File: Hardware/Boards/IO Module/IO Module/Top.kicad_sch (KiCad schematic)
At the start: 0 parts

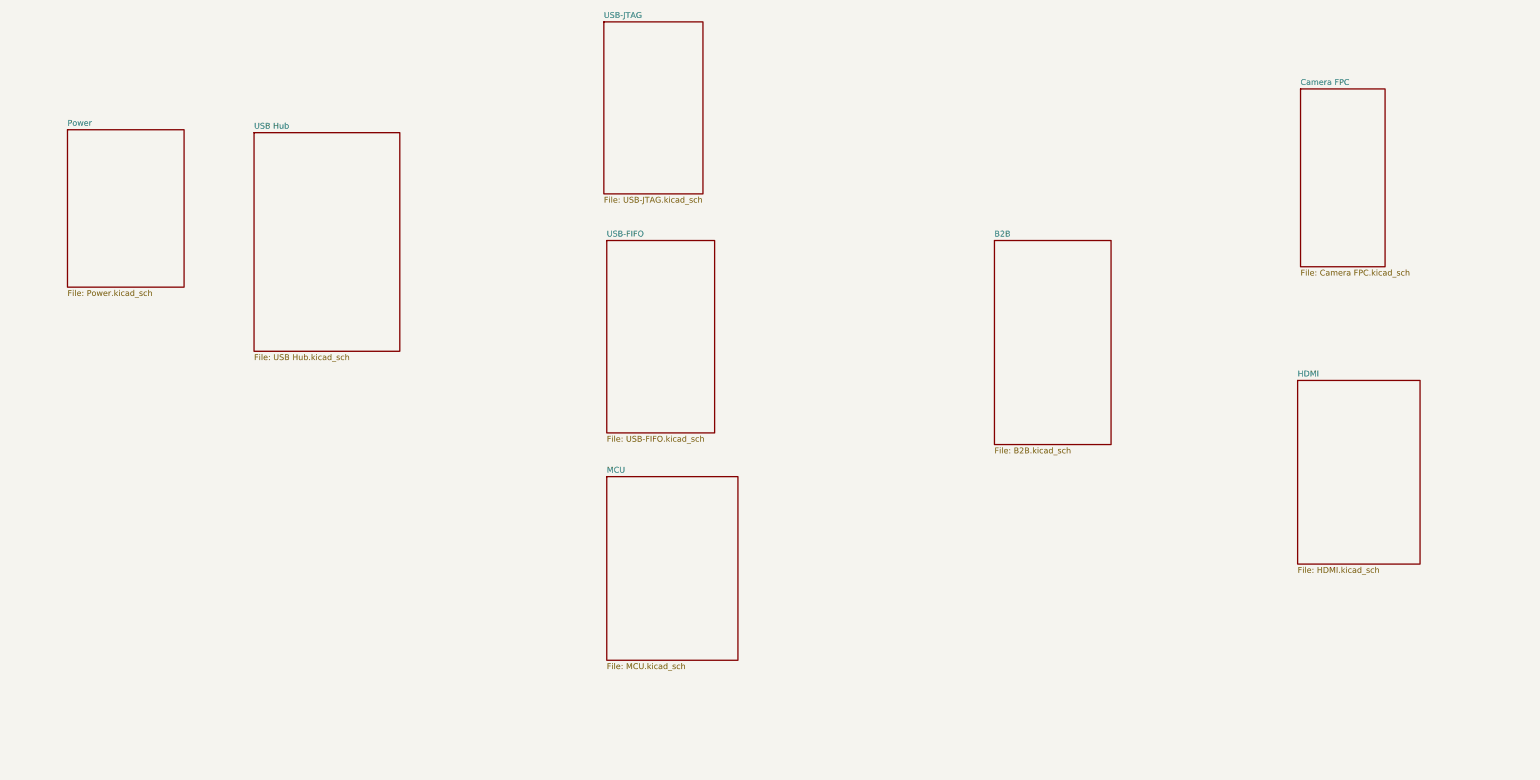
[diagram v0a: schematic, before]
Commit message: Completed IO Module Schematics
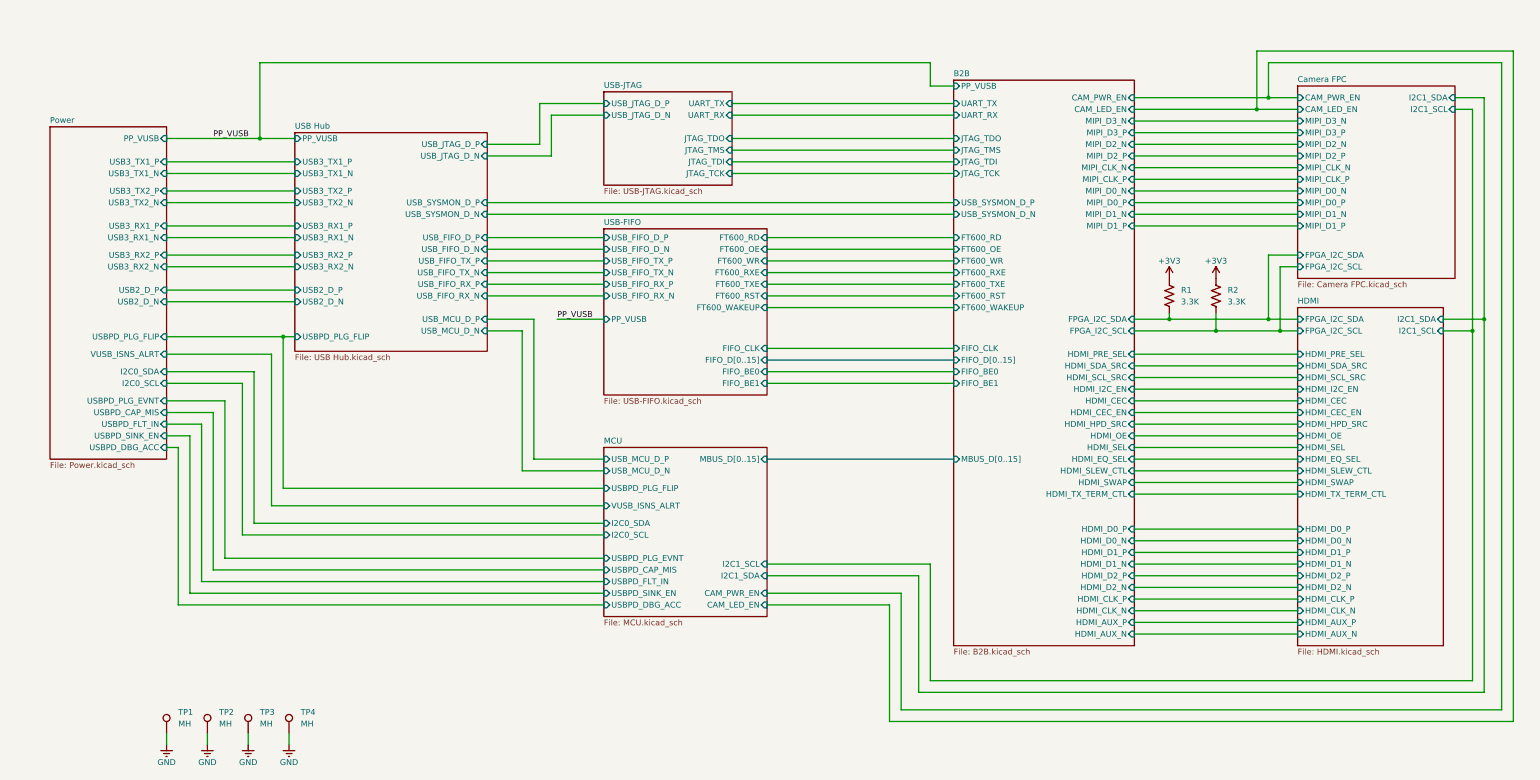
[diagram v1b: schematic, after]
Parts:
- added R1, R2: 3.3K, Resistor_SMD:R_0402_1005Metric, symbol Device:R_US
- added TP1, TP2, TP3, TP4: MH, MountingHole:MountingHole_2.2mm_M2_Pad_Via, symbol Connector:TestPoint
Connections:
- new net +3V3: R1.2, R2.2
- new net B2B/FPGA_I2C_SCL: R2.1
- new net B2B/FPGA_I2C_SDA: R1.1
- new net GND: TP1.1, TP2.1, TP3.1, TP4.1
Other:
- sheet B2B ports: added CAM_LED_EN, CAM_PWR_EN, FIFO_BE0, FIFO_BE1, FIFO_CLK, FIFO_D[0..15], FPGA_I2C_SCL, FPGA_I2C_SDA, FT600_OE, FT600_RD, FT600_RST, FT600_RXE, FT600_TXE, FT600_WAKEUP, FT600_WR, HDMI_AUX_N, HDMI_AUX_P, HDMI_CEC, HDMI_CEC_EN, HDMI_CLK_N, HDMI_CLK_P, HDMI_D0_N, HDMI_D0_P, HDMI_D1_N, HDMI_D1_P, HDMI_D2_N, HDMI_D2_P, HDMI_EQ_SEL, HDMI_HPD_SRC, HDMI_I2C_EN, HDMI_OE, HDMI_PRE_SEL, HDMI_SCL_SRC, HDMI_SDA_SRC, HDMI_SEL, HDMI_SLEW_CTL, HDMI_SWAP, HDMI_TX_TERM_CTL, JTAG_TCK, JTAG_TDI, JTAG_TDO, JTAG_TMS, MBUS_D[0..15], MIPI_CLK_N, MIPI_CLK_P, MIPI_D0_N, MIPI_D0_P, MIPI_D1_N, MIPI_D1_P, MIPI_D2_N, MIPI_D2_P, MIPI_D3_N, MIPI_D3_P, PP_VUSB, UART_RX, UART_TX, USB_SYSMON_D_N, USB_SYSMON_D_P; removed none
- sheet Camera FPC ports: added CAM_LED_EN, CAM_PWR_EN, FPGA_I2C_SCL, FPGA_I2C_SDA, I2C1_SCL, I2C1_SDA, MIPI_CLK_N, MIPI_CLK_P, MIPI_D0_N, MIPI_D0_P, MIPI_D1_N, MIPI_D1_P, MIPI_D2_N, MIPI_D2_P, MIPI_D3_N, MIPI_D3_P; removed none
- sheet HDMI ports: added FPGA_I2C_SCL, FPGA_I2C_SDA, HDMI_AUX_N, HDMI_AUX_P, HDMI_CEC, HDMI_CEC_EN, HDMI_CLK_N, HDMI_CLK_P, HDMI_D0_N, HDMI_D0_P, HDMI_D1_N, HDMI_D1_P, HDMI_D2_N, HDMI_D2_P, HDMI_EQ_SEL, HDMI_HPD_SRC, HDMI_I2C_EN, HDMI_OE, HDMI_PRE_SEL, HDMI_SCL_SRC, HDMI_SDA_SRC, HDMI_SEL, HDMI_SLEW_CTL, HDMI_SWAP, HDMI_TX_TERM_CTL, I2C1_SCL, I2C1_SDA; removed none
- sheet MCU ports: added CAM_LED_EN, CAM_PWR_EN, I2C0_SCL, I2C0_SDA, I2C1_SCL, I2C1_SDA, MBUS_D[0..15], USBPD_CAP_MIS, USBPD_DBG_ACC, USBPD_FLT_IN, USBPD_PLG_EVNT, USBPD_PLG_FLIP, USBPD_SINK_EN, USB_MCU_D_N, USB_MCU_D_P, VUSB_ISNS_ALRT; removed none
- sheet Power ports: added I2C0_SCL, I2C0_SDA, PP_VUSB, USB2_D_N, USB2_D_P, USB3_RX1_N, USB3_RX1_P, USB3_RX2_N, USB3_RX2_P, USB3_TX1_N, USB3_TX1_P, USB3_TX2_N, USB3_TX2_P, USBPD_CAP_MIS, USBPD_DBG_ACC, USBPD_FLT_IN, USBPD_PLG_EVNT, USBPD_PLG_FLIP, USBPD_SINK_EN, VUSB_ISNS_ALRT; removed none
- sheet USB Hub ports: added PP_VUSB, USB2_D_N, USB2_D_P, USB3_RX1_N, USB3_RX1_P, USB3_RX2_N, USB3_RX2_P, USB3_TX1_N, USB3_TX1_P, USB3_TX2_N, USB3_TX2_P, USBPD_PLG_FLIP, USB_FIFO_D_N, USB_FIFO_D_P, USB_FIFO_RX_N, USB_FIFO_RX_P, USB_FIFO_TX_N, USB_FIFO_TX_P, USB_JTAG_D_N, USB_JTAG_D_P, USB_MCU_D_N, USB_MCU_D_P, USB_SYSMON_D_N, USB_SYSMON_D_P; removed none
- sheet USB-FIFO ports: added FIFO_BE0, FIFO_BE1, FIFO_CLK, FIFO_D[0..15], FT600_OE, FT600_RD, FT600_RST, FT600_RXE, FT600_TXE, FT600_WAKEUP, FT600_WR, PP_VUSB, USB_FIFO_D_N, USB_FIFO_D_P, USB_FIFO_RX_N, USB_FIFO_RX_P, USB_FIFO_TX_N, USB_FIFO_TX_P; removed none
- sheet USB-JTAG ports: added JTAG_TCK, JTAG_TDI, JTAG_TDO, JTAG_TMS, UART_RX, UART_TX, USB_JTAG_D_N, USB_JTAG_D_P; removed none

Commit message: Updated SCH with notes & annotations
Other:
- sheet USB Hub ports: added USBPD_PLG_EVNT; removed none
- note added: "M2 Mounting Holes"

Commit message: Updated PCB routing for IO Module
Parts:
- R1, R2: footprint Resistor_SMD:R_0402_1005Metric -> Resistor_SMD:R_0201_0603Metric
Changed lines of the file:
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@@
 			)
 		)
-		(property "Footprint" "Resistor_SMD:R_0402_1005Metric"
+		(property "Footprint" "Resistor_SMD:R_0201_0603Metric"
 			(at 306.324 120.396 90)
 			(effects
@@
 			)
 		)
-		(property "Footprint" "Resistor_SMD:R_0402_1005Metric"
+		(property "Footprint" "Resistor_SMD:R_0201_0603Metric"
 			(at 296.164 120.396 90)
 			(effects

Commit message: Cleaned up routing for IO module
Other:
- sheet B2B ports: added MBUS_D[0..14]; removed MBUS_D[0..15]
- sheet HDMI ports: added HDMI_BUFF_EN; removed none
- sheet MCU ports: added HDMI_BUFF_EN, MBUS_D[0..14]; removed MBUS_D[0..15]
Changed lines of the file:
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@@
 	(wire
 		(pts
+			(xy 248.92 201.93) (xy 248.92 175.26)
+		)
+		(stroke
+			(width 0)
+			(type default)
+		)
+	)
+	(wire
+		(pts
 			(xy 209.55 118.11) (xy 250.19 118.11)
 		)
@@
 	(wire
 		(pts
+			(xy 248.92 175.26) (xy 209.55 175.26)
+		)
+		(stroke
+			(width 0)
+			(type default)
+		)
+	)
+	(wire
+		(pts
 			(xy 307.34 128.27) (xy 321.31 128.27)
 		)
@@
 	(wire
 		(pts
+			(xy 360.68 201.93) (xy 248.92 201.93)
+		)
+		(stroke
+			(width 0)
+			(type default)
+		)
+	)
+	(wire
+		(pts
 			(xy 289.56 97.79) (xy 325.12 97.79)
 		)
@@
 	(wire
 		(pts
+			(xy 360.68 133.35) (xy 360.68 201.93)
+		)
+		(stroke
+			(width 0)
+			(type default)
+		)
+	)
+	(wire
+		(pts
 			(xy 81.28 187.96) (xy 173.99 187.96)
 		)
@@
 	(wire
 		(pts
+			(xy 356.87 133.35) (xy 360.68 133.35)
+		)
+		(stroke
+			(width 0)
+			(type default)
+		)
+	)
+	(wire
+		(pts
 			(xy 242.57 181.61) (xy 242.57 207.01)
 		)
@@
 			)
 		)
-		(pin "MBUS_D[0..15]" input
-			(at 250.19 156.21 180)
-			(effects
-				(font
-					(size 1.27 1.27)
-				)
-				(justify left)
-			)
-		)
 		(pin "FIFO_D[0..15]" input
 			(at 250.19 134.62 180)
@@
 			)
 		)
+		(pin "MBUS_D[0..14]" input
+			(at 250.19 156.21 180)
+			(effects
+				(font
+					(size 1.27 1.27)
+				)
+				(justify left)
+			)
+		)
 		(instances
 			(project "IO Module"
@@
 			)
 		)
+		(pin "HDMI_BUFF_EN" input
+			(at 356.87 133.35 0)
+			(effects
+				(font
+					(size 1.27 1.27)
+				)
+				(justify right)
+			)
+		)
 		(instances
 			(project "IO Module"
@@
 			)
 		)
-		(pin "MBUS_D[0..15]" input
-			(at 209.55 156.21 0)
-			(effects
-				(font
-					(size 1.27 1.27)
-				)
-				(justify right)
-			)
-		)
 		(pin "CAM_PWR_EN" input
 			(at 209.55 185.42 0)
@@
 			)
 		)
+		(pin "MBUS_D[0..14]" input
+			(at 209.55 156.21 0)
+			(effects
+				(font
+					(size 1.27 1.27)
+				)
+				(justify right)
+			)
+		)
+		(pin "HDMI_BUFF_EN" input
+			(at 209.55 175.26 0)
+			(effects
+				(font
+					(size 1.27 1.27)
+				)
+				(justify right)
+			)
+		)

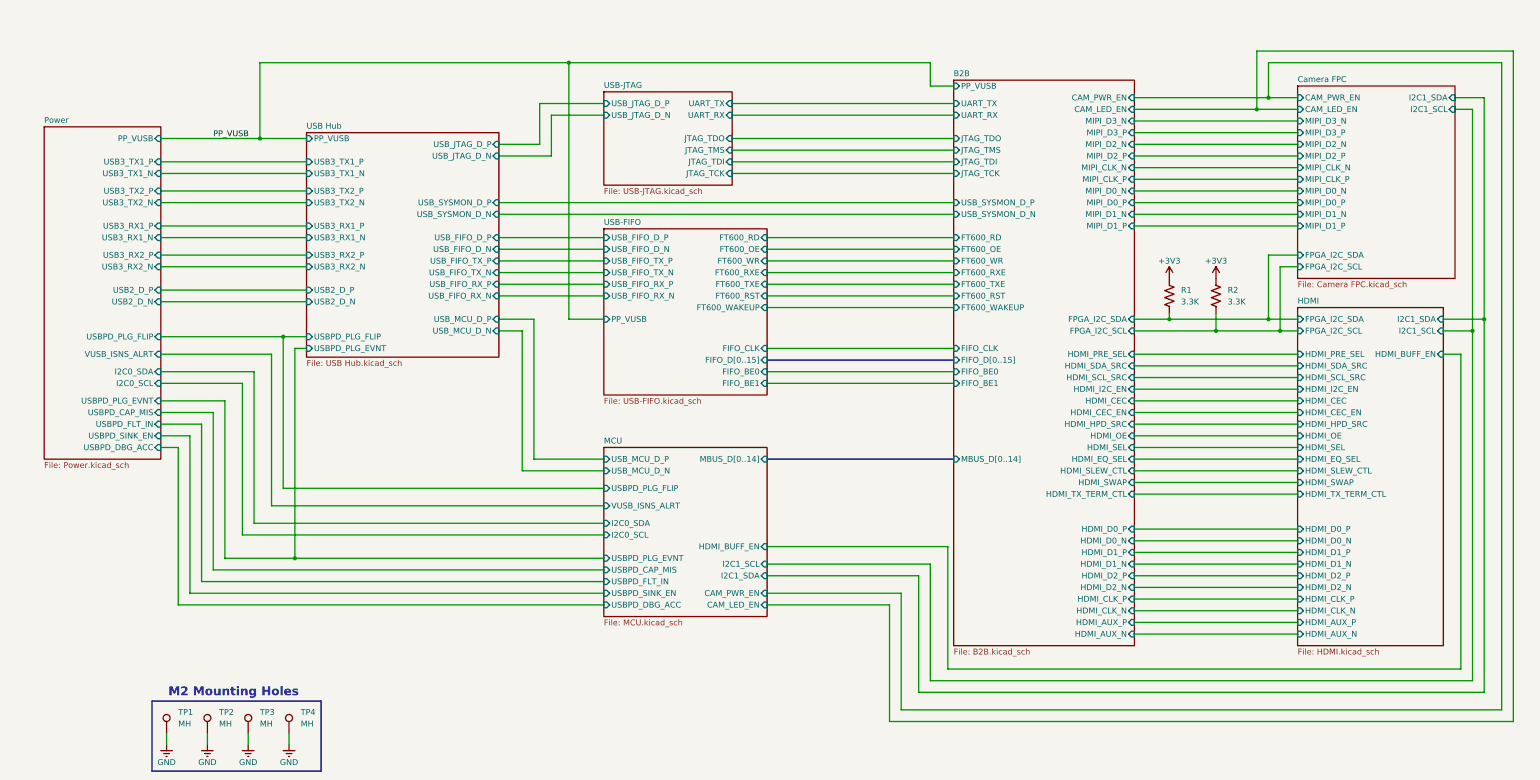
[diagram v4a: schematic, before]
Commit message: Using new DP to HDMI IC
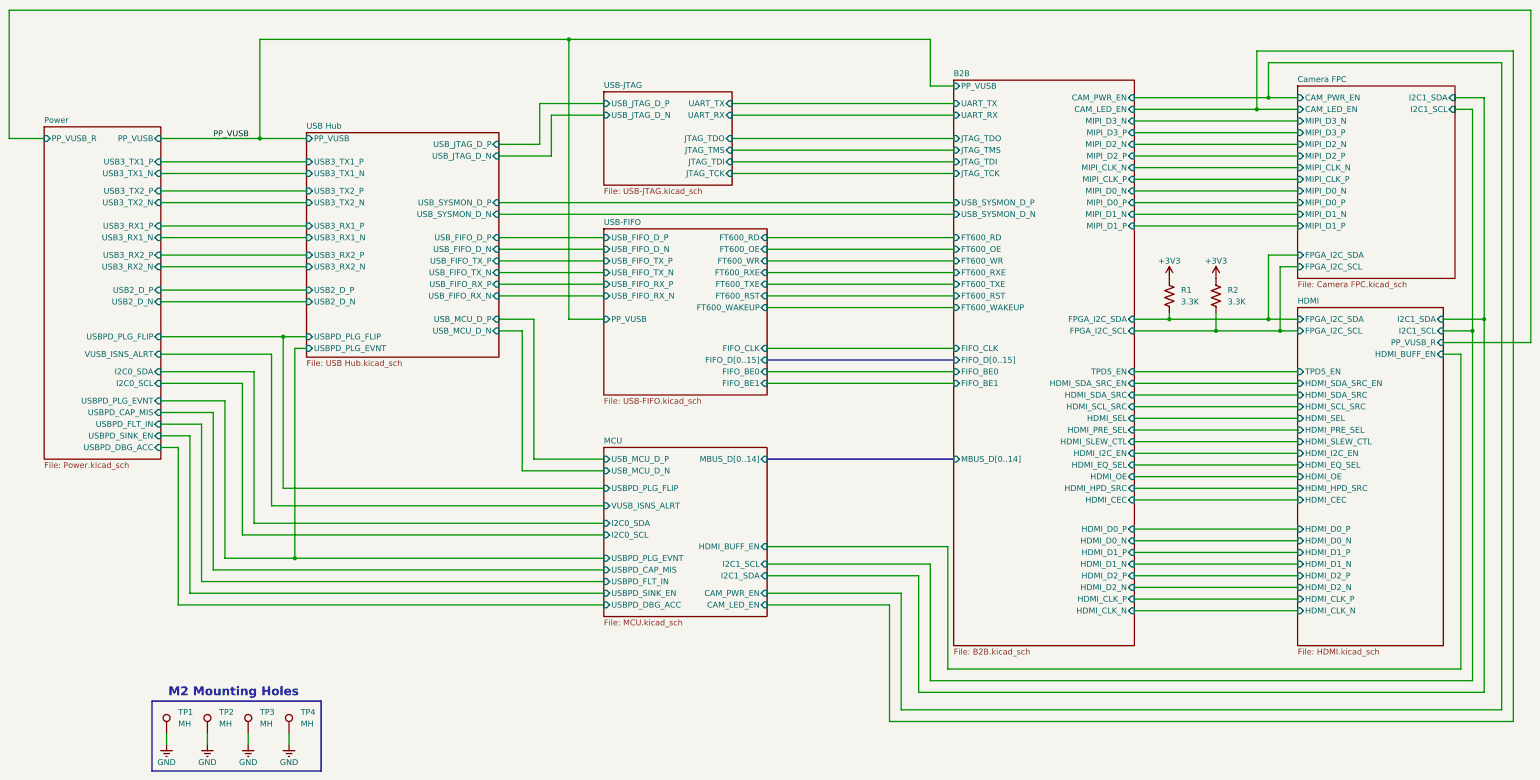
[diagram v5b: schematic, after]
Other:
- sheet B2B ports: added HDMI_SDA_SRC_EN, TPD5_EN; removed HDMI_AUX_N, HDMI_AUX_P, HDMI_CEC_EN, HDMI_SWAP, HDMI_TX_TERM_CTL
- sheet HDMI ports: added HDMI_SDA_SRC_EN, PP_VUSB_R, TPD5_EN; removed HDMI_AUX_N, HDMI_AUX_P, HDMI_CEC_EN, HDMI_SWAP, HDMI_TX_TERM_CTL
- sheet Power ports: added PP_VUSB_R; removed none
